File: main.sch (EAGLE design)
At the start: 31 parts

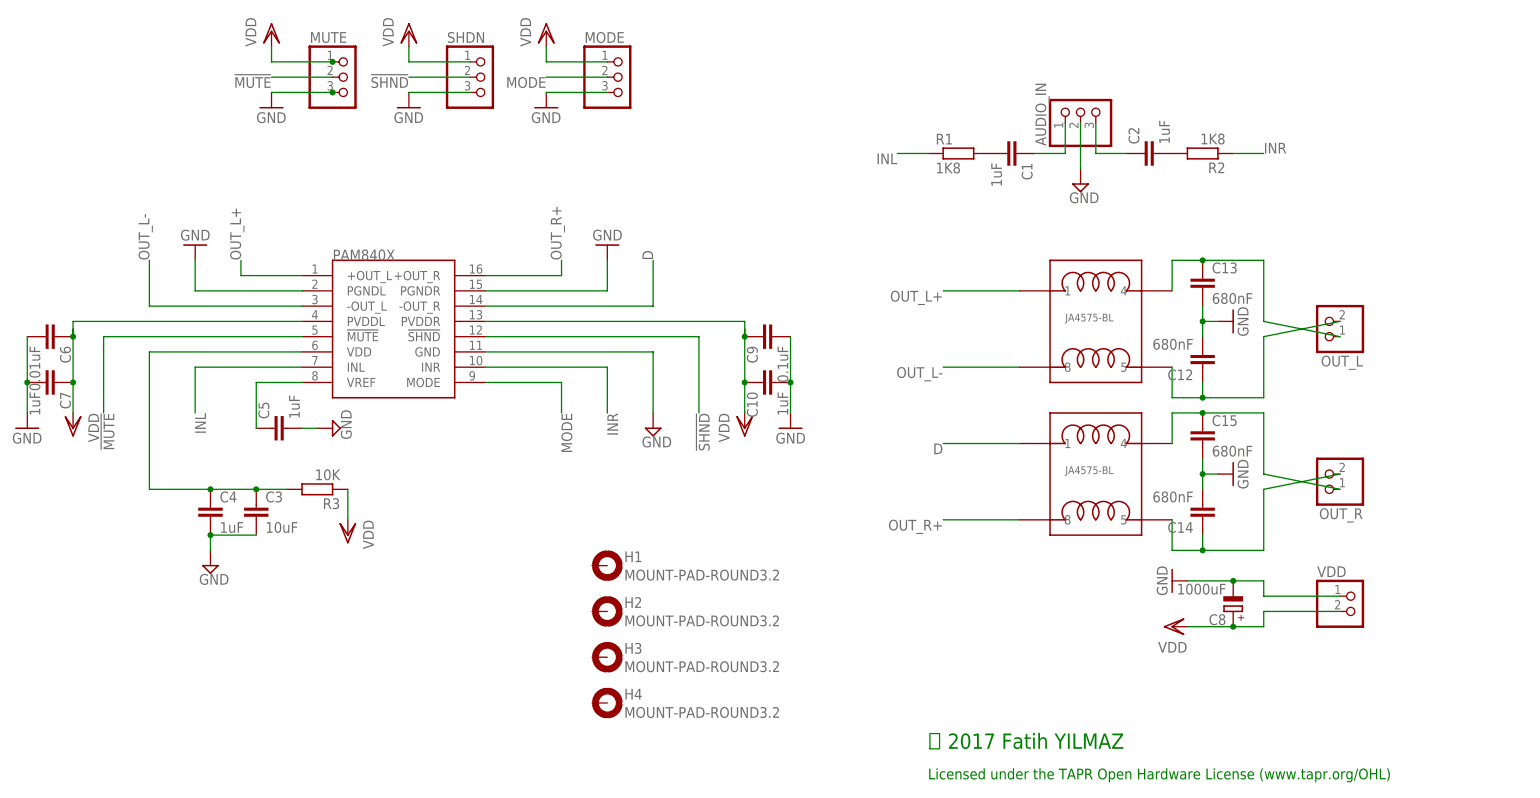
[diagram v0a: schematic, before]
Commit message: rev 2.0
board size's reduced, main bypass cap's size and value has changed.
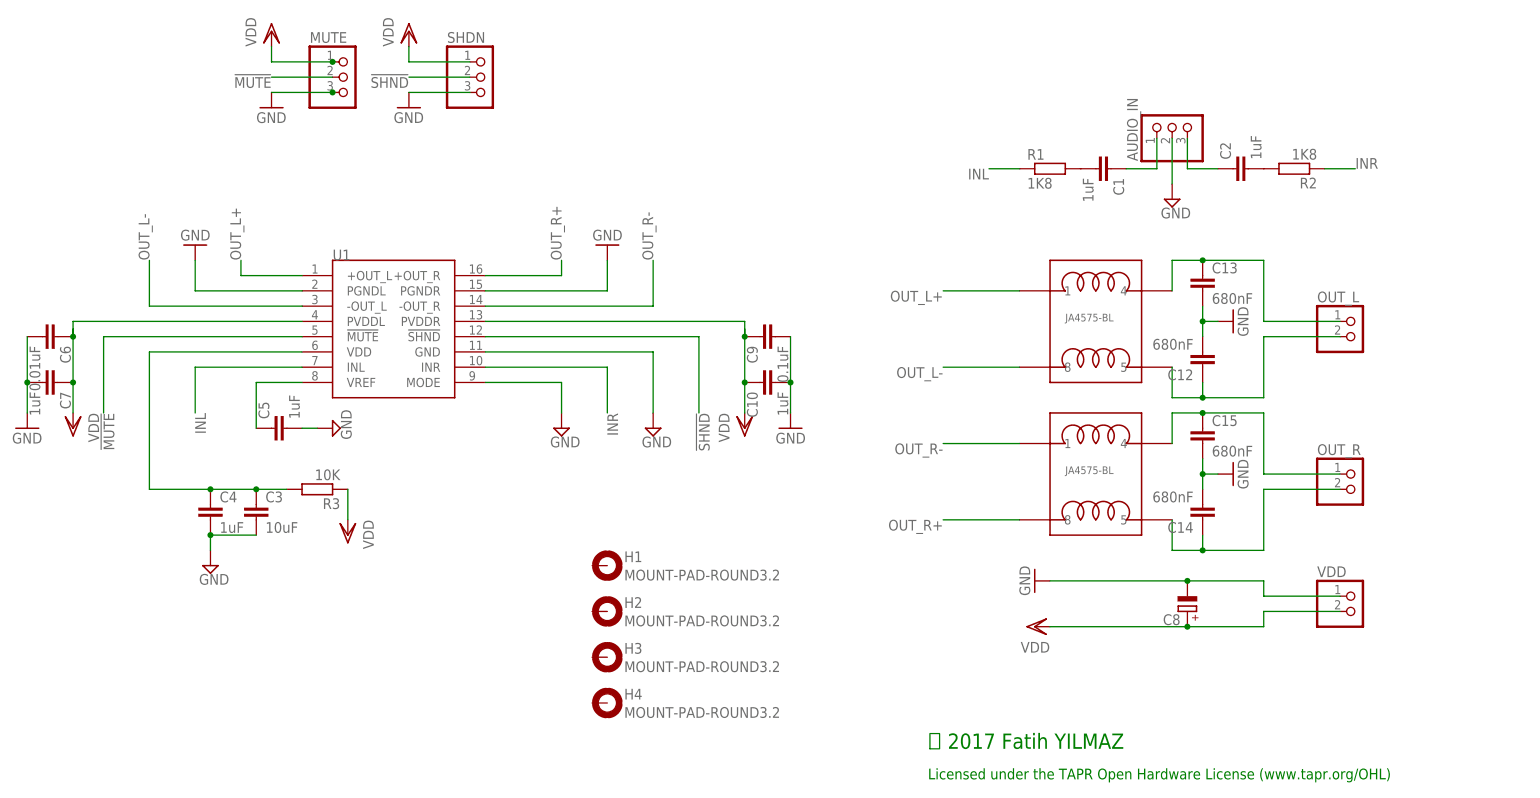
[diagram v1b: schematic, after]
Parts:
- removed MODE: (no value), pinhead:PINHD-1X3
- C8: value 1000uF -> (none); device rcl:CPOL-EUTAP5-45 -> rcl:CPOL-EUE3.5-8
- renumbered PAM840X to U1, U$1 to LEFT_COIL, U$2 to RIGHT_COIL
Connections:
- net D renamed OUT_R-
- removed net MODE: MODE.2, U1.MODE
- net GND: now also U1.MODE; no longer MODE.3
- net VDD: no longer MODE.1
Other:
- moved on the sheet: AUDIO_IN, C1, C2, C8, OUT_L, OUT_R, R1, R2

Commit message: New board design
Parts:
- removed AUDIO_IN, MUTE, SHDN: (no value), pinhead:PINHD-1X3
- removed VDD: (no value), pinhead:PINHD-1X2
- added C11: (no value), rcl:CPOL-EUE3.5-8
- added J1: (no value), SparkFun-Connectors:CONN_09NO_SILK
- C12, C13, C14, C15: device rcl:C-EU025-025X050 -> rcl:C-EU050-045X075
- H1, H2, H3, H4: value MOUNT-PAD-ROUND3.2 -> MOUNT-PAD-ROUND3.0; device holes:MOUNT-PAD-ROUND3.2 -> holes:MOUNT-PAD-ROUND3.0
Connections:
- removed net !MUTE: MUTE.2, U1.!MUTE
- removed net !SHND: SHDN.2, U1.!SHND
- new net MUTE: J1.3, U1.!MUTE
- new net SHDN: J1.7, U1.!SHND
- net GND: now also C11.-, H1.MOUNT, H2.MOUNT, H3.MOUNT, H4.MOUNT, J1.2, J1.5, J1.8; no longer AUDIO_IN.2, MUTE.3, SHDN.3, VDD.1
- net N$3: now also J1.4; no longer AUDIO_IN.1
- net N$5: now also J1.6; no longer AUDIO_IN.3
- net VDD: now also C11.+, J1.1, J1.9; no longer MUTE.1, SHDN.1, VDD.2
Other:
- moved on the sheet: C8
